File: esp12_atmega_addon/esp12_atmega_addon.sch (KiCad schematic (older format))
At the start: 11 parts, among them U1 ESP-12E, U2 ATMEGA328P-MU

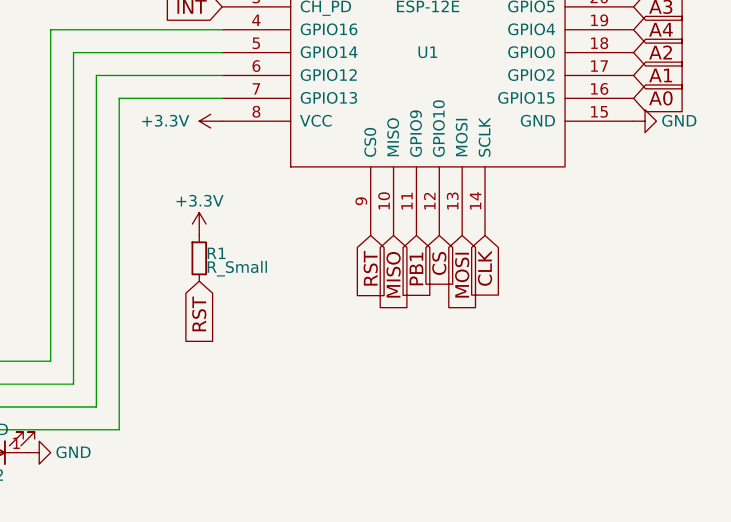
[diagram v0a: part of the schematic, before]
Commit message: Fixed DRC violations and changed the pinout a little bit
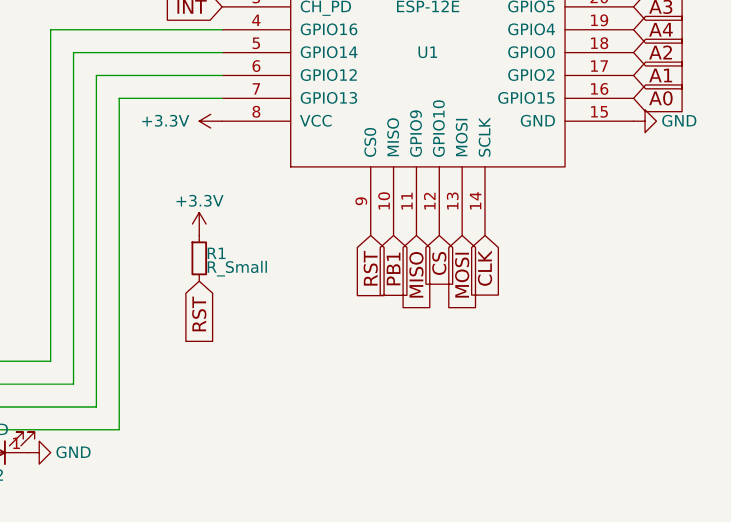
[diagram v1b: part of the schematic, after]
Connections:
- net MISO: now also U1.11 (GPIO9); no longer U1.10 (MISO)
- net PB1: now also U1.10 (MISO); no longer U1.11 (GPIO9)
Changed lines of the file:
@@
 LIBS:valves
 LIBS:ESP8266
+LIBS:esp12_atmega_addon-cache
 EELAYER 25 0
 EELAYER END
@@
 Text GLabel 5750 3450 3    60   Input ~ 0
 RST
-Text GLabel 5850 3450 3    60   Input ~ 0
+Text GLabel 5950 3450 3    60   Input ~ 0
 MISO
 Text GLabel 6150 3450 3    60   Input ~ 0
@@
 Text GLabel 3750 2200 2    60   Input ~ 0
 PB1
-Text GLabel 5950 3450 3    60   Input ~ 0
+Text GLabel 5850 3450 3    60   Input ~ 0
 PB1
 Text GLabel 3750 3900 2    60   Input ~ 0

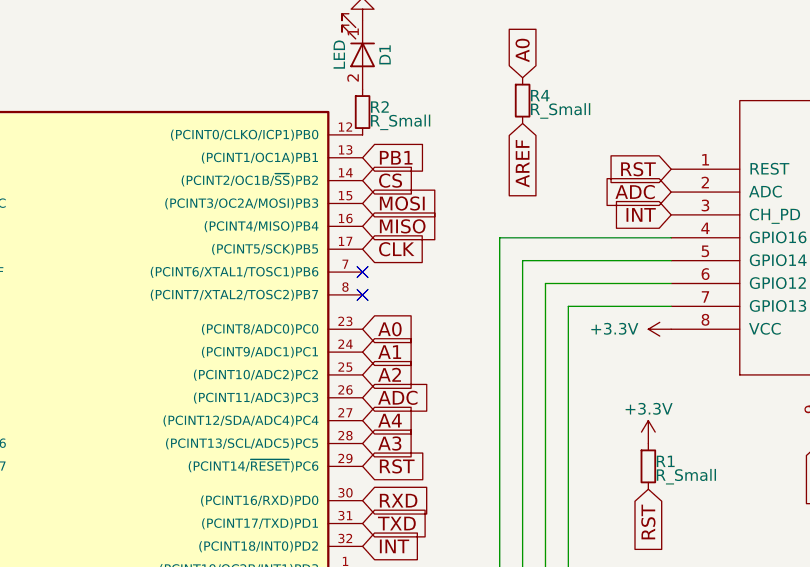
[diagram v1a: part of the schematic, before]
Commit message: Tying XTAL pins to ground
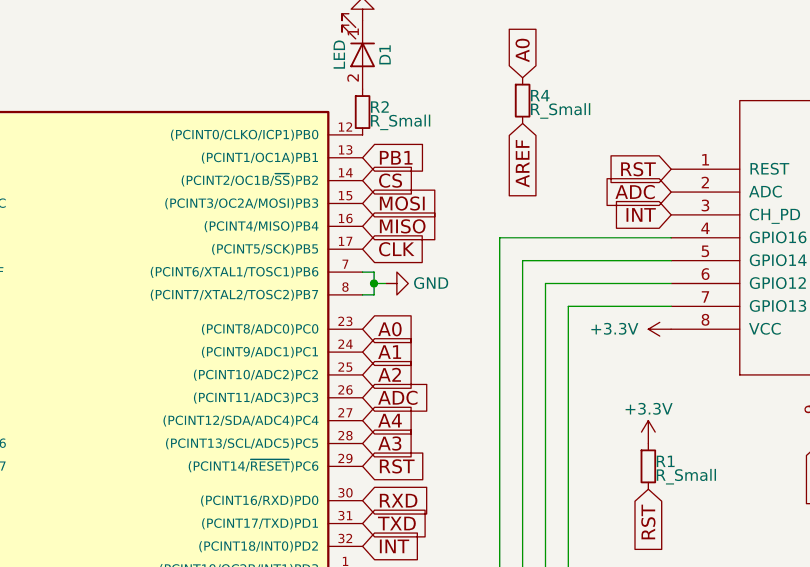
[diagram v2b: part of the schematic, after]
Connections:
- net GND: now also U2.7 ((PCINT6/XTAL1/TOSC1)PB6), U2.8 ((PCINT7/XTAL2/TOSC2)PB7)
- no-connect marks 4 -> 2
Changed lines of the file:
@@
 $EndComp
 $Comp
-L +3.3V #PWR15
+L +3.3V #PWR01
 U 1 1 596E7D62
 P 5100 2950
-F 0 "#PWR15" H 5100 2800 50  0001 C CNN
+F 0 "#PWR01" H 5100 2800 50  0001 C CNN
 F 1 "+3.3V" V 5100 3200 50  0000 C CNN
 F 2 "" H 5100 2950 50  0001 C CNN
@@
 $EndComp
 $Comp
-L GND #PWR16
+L GND #PWR02
 U 1 1 596E7D92
 P 6900 2950
-F 0 "#PWR16" H 6900 2700 50  0001 C CNN
+F 0 "#PWR02" H 6900 2700 50  0001 C CNN
 F 1 "GND" V 6900 2750 50  0000 C CNN
 F 2 "" H 6900 2950 50  0001 C CNN
@@
 $EndComp
 $Comp
-L GND #PWR9
+L GND #PWR03
 U 1 1 596E7EA6
 P 1850 4200
-F 0 "#PWR9" H 1850 3950 50  0001 C CNN
+F 0 "#PWR03" H 1850 3950 50  0001 C CNN
 F 1 "GND" V 1850 4000 50  0000 C CNN
 F 2 "" H 1850 4200 50  0001 C CNN
@@
 $EndComp
 $Comp
-L GND #PWR10
+L GND #PWR04
 U 1 1 596E7EEA
 P 1850 4300
-F 0 "#PWR10" H 1850 4050 50  0001 C CNN
+F 0 "#PWR04" H 1850 4050 50  0001 C CNN
 F 1 "GND" V 1850 4100 50  0000 C CNN
 F 2 "" H 1850 4300 50  0001 C CNN
@@
 $EndComp
 $Comp
-L GND #PWR11
+L GND #PWR05
 U 1 1 596E7EFB
 P 1850 4400
-F 0 "#PWR11" H 1850 4150 50  0001 C CNN
+F 0 "#PWR05" H 1850 4150 50  0001 C CNN
 F 1 "GND" V 1850 4200 50  0000 C CNN
 F 2 "" H 1850 4400 50  0001 C CNN
@@
 $EndComp
 $Comp
-L +3.3V #PWR6
+L +3.3V #PWR06
 U 1 1 596E7F3C
 P 1850 2100
-F 0 "#PWR6" H 1850 1950 50  0001 C CNN
+F 0 "#PWR06" H 1850 1950 50  0001 C CNN
 F 1 "+3.3V" V 1850 2350 50  0000 C CNN
 F 2 "" H 1850 2100 50  0001 C CNN
@@
 $EndComp
 $Comp
-L +3.3V #PWR7
+L +3.3V #PWR07
 U 1 1 596E7F74
 P 1850 2200
-F 0 "#PWR7" H 1850 2050 50  0001 C CNN
+F 0 "#PWR07" H 1850 2050 50  0001 C CNN
 F 1 "+3.3V" V 1850 2450 50  0000 C CNN
 F 2 "" H 1850 2200 50  0001 C CNN
@@
 $EndComp
 $Comp
-L +3.3V #PWR8
+L +3.3V #PWR08
 U 1 1 596E7F85
 P 1850 2400
-F 0 "#PWR8" H 1850 2250 50  0001 C CNN
+F 0 "#PWR08" H 1850 2250 50  0001 C CNN
 F 1 "+3.3V" V 1850 2650 50  0000 C CNN
 F 2 "" H 1850 2400 50  0001 C CNN
@@
 $EndComp
 $Comp
-L GND #PWR5
+L GND #PWR09
 U 1 1 596E7FCB
 P 1600 2950
-F 0 "#PWR5" H 1600 2700 50  0001 C CNN
+F 0 "#PWR09" H 1600 2700 50  0001 C CNN
 F 1 "GND" H 1600 2800 50  0000 C CNN
 F 2 "" H 1600 2950 50  0001 C CNN
@@
 $EndComp
 $Comp
-L GND #PWR2
+L GND #PWR010
 U 1 1 596E85D5
 P 850 2950
-F 0 "#PWR2" H 850 2700 50  0001 C CNN
+F 0 "#PWR010" H 850 2700 50  0001 C CNN
 F 1 "GND" V 850 2750 50  0000 C CNN
 F 2 "" H 850 2950 50  0001 C CNN
@@
 $EndComp
 $Comp
-L +3.3V #PWR1
+L +3.3V #PWR011
 U 1 1 596E85EC
 P 850 2750
-F 0 "#PWR1" H 850 2600 50  0001 C CNN
+F 0 "#PWR011" H 850 2600 50  0001 C CNN
 F 1 "+3.3V" V 850 3000 50  0000 C CNN
 F 2 "" H 850 2750 50  0001 C CNN
@@
 $EndComp
 $Comp
-L GND #PWR4
+L GND #PWR012
 U 1 1 596E8648
 P 1200 2950
-F 0 "#PWR4" H 1200 2700 50  0001 C CNN
+F 0 "#PWR012" H 1200 2700 50  0001 C CNN
 F 1 "GND" V 1200 2750 50  0000 C CNN
 F 2 "" H 1200 2950 50  0001 C CNN
@@
 $EndComp
 $Comp
-L +3.3V #PWR3
+L +3.3V #PWR013
 U 1 1 596E864E
 P 1200 2750
-F 0 "#PWR3" H 1200 2600 50  0001 C CNN
+F 0 "#PWR013" H 1200 2600 50  0001 C CNN
 F 1 "+3.3V" V 1200 3000 50  0000 C CNN
 F 2 "" H 1200 2750 50  0001 C CNN
@@
 $EndComp
 $Comp
-L +3.3V #PWR14
+L +3.3V #PWR014
 U 1 1 596E8C02
 P 5000 3450
-F 0 "#PWR14" H 5000 3300 50  0001 C CNN
+F 0 "#PWR014" H 5000 3300 50  0001 C CNN
 F 1 "+3.3V" H 5000 3600 50  0000 C CNN
 F 2 "" H 5000 3450 50  0001 C CNN
@@
 $EndComp
 $Comp
-L GND #PWR13
+L GND #PWR015
 U 1 1 596E920E
 P 4250 4400
-F 0 "#PWR13" H 4250 4150 50  0001 C CNN
+F 0 "#PWR015" H 4250 4150 50  0001 C CNN
 F 1 "GND" V 4250 4200 50  0000 C CNN
 F 2 "" H 4250 4400 50  0001 C CNN
@@
 $EndComp
 $Comp
-L GND #PWR12
+L GND #PWR016
 U 1 1 596E9237
 P 3750 1600
-F 0 "#PWR12" H 3750 1350 50  0001 C CNN
+F 0 "#PWR016" H 3750 1350 50  0001 C CNN
 F 1 "GND" H 3750 1450 50  0000 C CNN
 F 2 "" H 3750 1600 50  0001 C CNN
@@
 	-1   0    0    1
 $EndComp
-NoConn ~ 3750 2700
-NoConn ~ 3750 2800
 NoConn ~ 1850 3450
 NoConn ~ 1850 3550
@@
 Text GLabel 4450 2050 3    60   Input ~ 0
 AREF
+$Comp
+L GND #PWR017
+U 1 1 5AFC3527
+P 3850 2750
+F 0 "#PWR017" H 3850 2500 50  0001 C CNN
+F 1 "GND" V 3850 2550 50  0000 C CNN
+F 2 "" H 3850 2750 50  0001 C CNN
+F 3 "" H 3850 2750 50  0001 C CNN
+	1    3850 2750
+	0    -1   -1   0
+$EndComp
+Wire Wire Line
+	3750 2700 3800 2700
+Wire Wire Line
+	3800 2700 3800 2800
+Wire Wire Line
+	3800 2800 3750 2800
+Wire Wire Line
+	3800 2750 3850 2750
+Connection ~ 3800 2750
 $EndSCHEMATC
